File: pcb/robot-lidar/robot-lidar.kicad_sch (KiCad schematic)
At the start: 1 part, among them U1 STM32F429VETx

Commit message: add jack
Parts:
- added J1: Barrel_Jack, symbol Connector:Barrel_Jack
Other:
- moved on the sheet: U1
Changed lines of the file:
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@@
 (kicad_sch (version 20230121) (generator eeschema)
   (paper "A4")
-  (symbol (lib_id "MCU_ST_STM32F4:STM32F429VETx") (at 90.17 99.06 0) (unit 1)
+  (symbol (lib_id "MCU_ST_STM32F4:STM32F429VETx") (at 77.47 113.03 0) (unit 1)
     (in_bom yes) (on_board yes) (dnp no) (fields_autoplaced)
-    (property "Reference" "U1" (at 94.9041 167.64 0)
+    (property "Reference" "U1" (at 82.2041 181.61 0)
       (effects (font (size 1.27 1.27)) (justify left))
     )
-    (property "Value" "STM32F429VETx" (at 94.9041 170.18 0)
+    (property "Value" "STM32F429VETx" (at 82.2041 184.15 0)
       (effects (font (size 1.27 1.27)) (justify left))
     )
-    (property "Footprint" "Package_QFP:LQFP-100_14x14mm_P0.5mm" (at 72.39 165.1 0)
+    (property "Footprint" "Package_QFP:LQFP-100_14x14mm_P0.5mm" (at 59.69 179.07 0)
       (effects (font (size 1.27 1.27)) (justify right) hide)
     )
-    (property "Datasheet" "https://www.st.com/resource/en/datasheet/stm32f429ve.pdf" (at 90.17 99.06 0)
+    (property "Datasheet" "https://www.st.com/resource/en/datasheet/stm32f429ve.pdf" (at 77.47 113.03 0)
       (effects (font (size 1.27 1.27)) hide)
     )
@@
         )
       )
+    )
+  )
+  (symbol (lib_id "Connector:Barrel_Jack") (at 22.86 24.13 0) (unit 1)
+    (in_bom yes) (on_board yes) (dnp no) (fields_autoplaced)
+    (property "Reference" "J1" (at 22.86 15.24 0)
+      (effects (font (size 1.27 1.27)))
+    )
+    (property "Value" "Barrel_Jack" (at 22.86 17.78 0)
+      (effects (font (size 1.27 1.27)))
+    )
+    (property "Footprint" "" (at 24.13 25.146 0)
+      (effects (font (size 1.27 1.27)) hide)
+    )
+    (property "Datasheet" "~" (at 24.13 25.146 0)
+      (effects (font (size 1.27 1.27)) hide)
+    )
+    (pin "1")
+    (pin "2")
+    (instances
+      (project "robot-lidar"
+        (path "/cb10bbf7-c2c1-4a0d-8947-ad707931d83b"
+          (reference "J1") (unit 1)
+        )
+      )

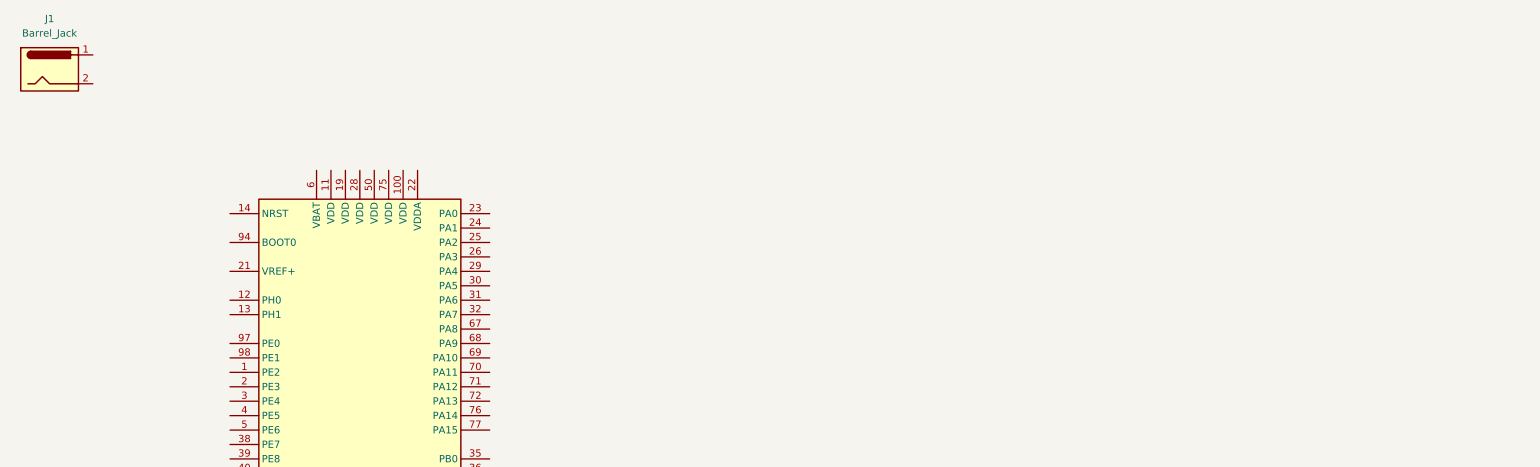
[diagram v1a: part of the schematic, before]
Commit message: add libar + regulator
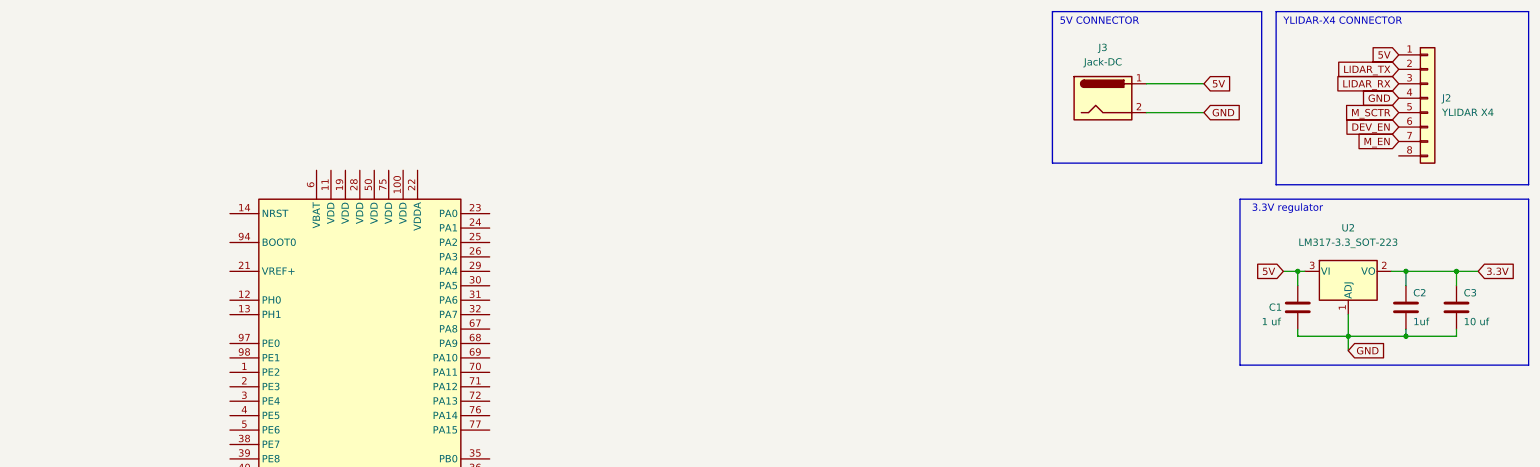
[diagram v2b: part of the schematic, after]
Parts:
- removed J1: Barrel_Jack, symbol Connector:Barrel_Jack
- added C1: 1 uf, Capacitor_SMD:C_0603_1608Metric, symbol Device:C
- added C2: 1uf, Capacitor_SMD:C_0603_1608Metric, symbol Device:C
- added C3: 10 uf, Capacitor_SMD:C_0603_1608Metric, symbol Device:C
- added J2: YLIDAR X4, Connector_Hirose:Hirose_DF13-08P-1.25DSA_1x08_P1.25mm_Vertical, symbol Connector_Generic:Conn_01x08
- added J3: Jack-DC, Connector_BarrelJack:BarrelJack_Horizontal, symbol Connector:Jack-DC
- added U2: LM317-3.3_SOT-223, Package_TO_SOT_SMD:SOT-223-3_TabPin2, symbol Regulator_Linear:LM317_SOT-223
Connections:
- new net 3.3V: C2.1, C3.1, U2.2 (VO)
- new net 5V: C1.1, J2.1 (Pin_1), J3.1, U2.3 (VI)
- new net DEV_EN: J2.6 (Pin_6)
- new net GND: C1.2, C2.2, C3.2, J2.4 (Pin_4), J3.2, U2.1 (ADJ)
- new net LIDAR_RX: J2.3 (Pin_3)
- new net LIDAR_TX: J2.2 (Pin_2)
- new net M_EN: J2.7 (Pin_7)
- new net M_SCTR: J2.5 (Pin_5)
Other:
- note added: "3.3V regulator"
- note added: "5V CONNECTOR"
- note added: "YLIDAR-X4 CONNECTOR"

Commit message: add gyro
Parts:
- added C1, C2, C3: C, Capacitor_SMD:C_0603_1608Metric, symbol Device:C
- added C4, C5, C6, C7, C8: 1 uf, Capacitor_SMD:C_0603_1608Metric, symbol Device:C
- added R1, R2: R_Small, Resistor_SMD:R_0603_1608Metric, symbol Device:R_Small
- added U2: MPU-6050, Sensor_Motion:InvenSense_QFN-24_4x4mm_P0.5mm, symbol Sensor_Motion:MPU-6050
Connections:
- net GND: now also C1.1, C2.2, C3.2, C4.2, C5.2, C6.2, C7.2, C8.2, U2.1 (CLKIN), U2.11 (FSYNC), U2.18 (GND), U2.9 (AD0)
- net at U1.100 (VDD): now also U1.11 (VDD), U1.19 (VDD), U1.22 (VDDA), U1.28 (VDD), U1.50 (VDD), U1.75 (VDD), C4.1, C5.1, C6.1, C7.1, C8.1
- new net: C3.1, U2.20 (CPOUT)
- new net: C2.1, U2.10 (REGOUT)
- new net +3V3: C1.2, R1.1, R2.1, U2.13 (VDD), U2.8 (VDDIO)
- new net MPU_IRQ: U2.12 (INT)
- new net SCL: R1.2, U2.23 (SCL)
- new net SDA: R2.2, U2.24 (SDA)
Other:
- note added: "MPU6050"

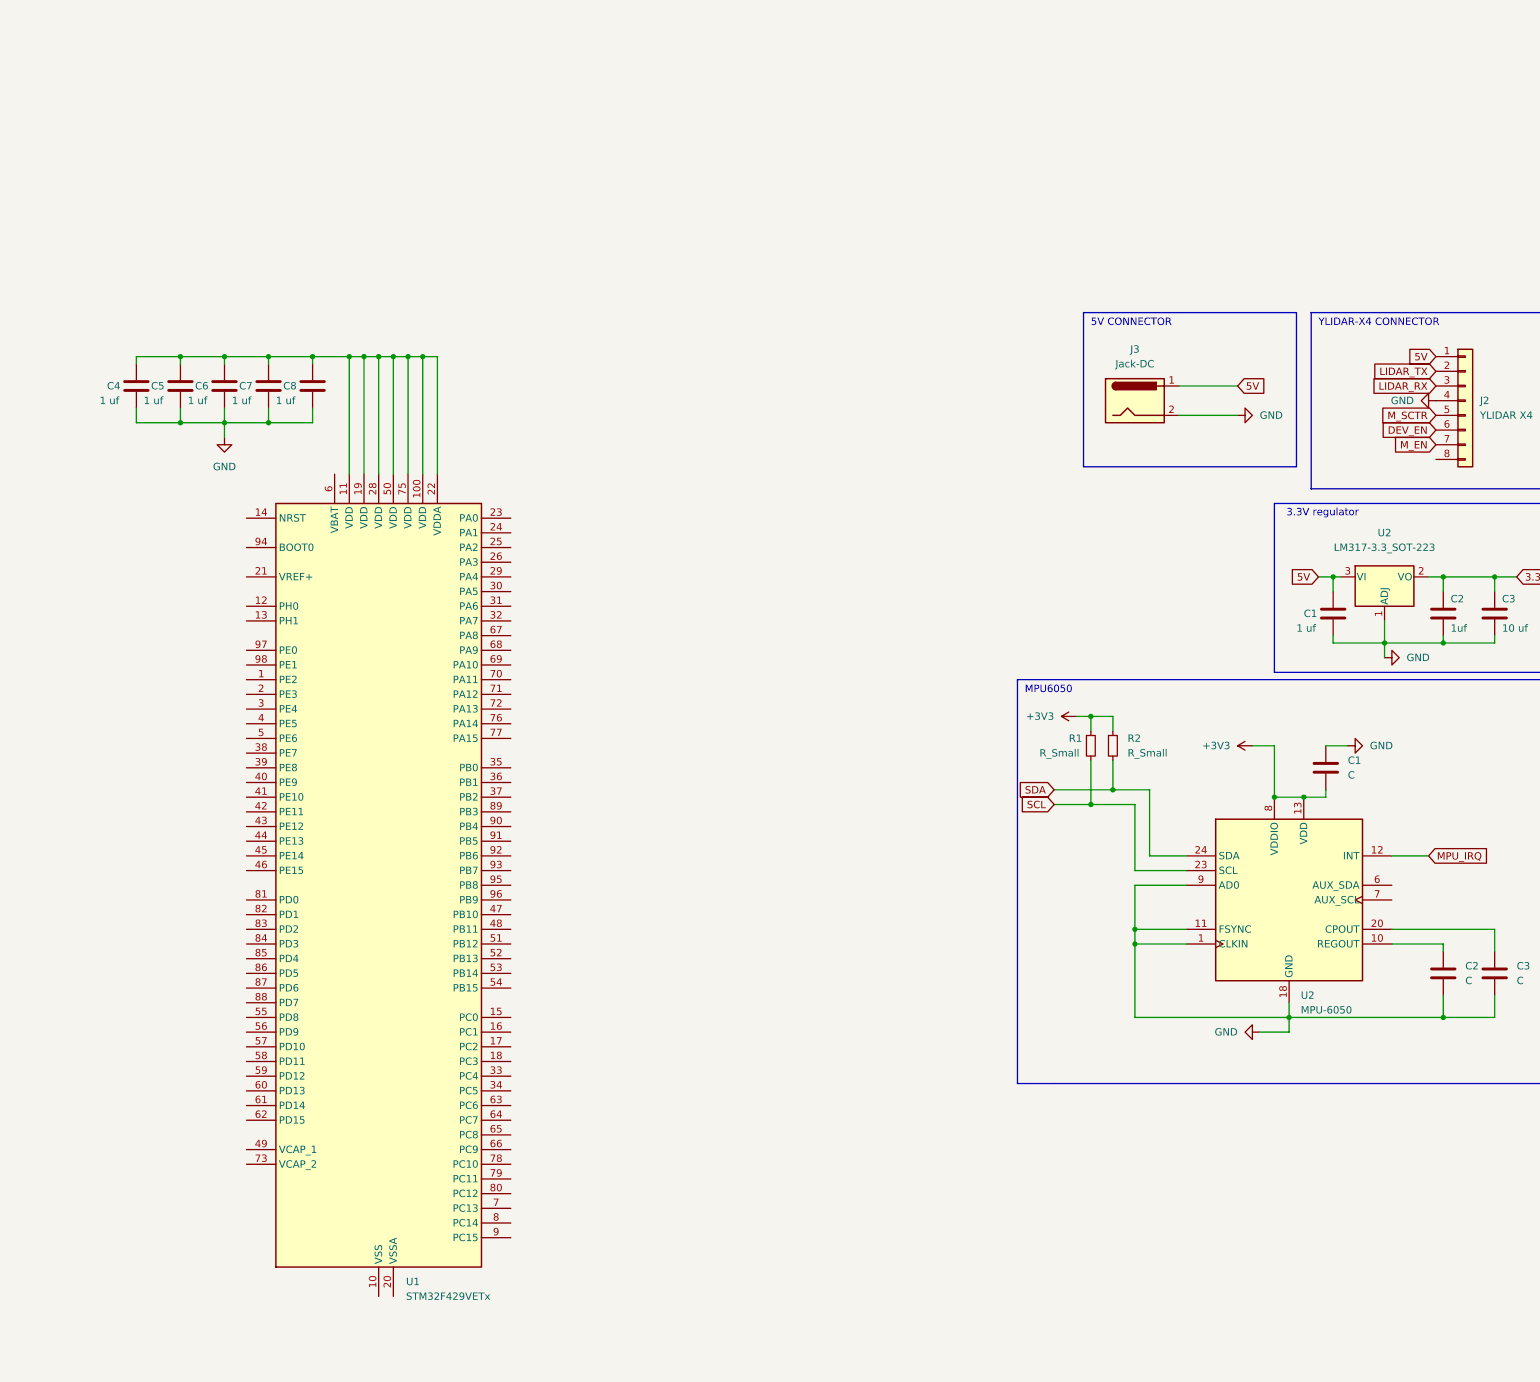
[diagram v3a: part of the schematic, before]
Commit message: add i2c pin + crystal + SWD
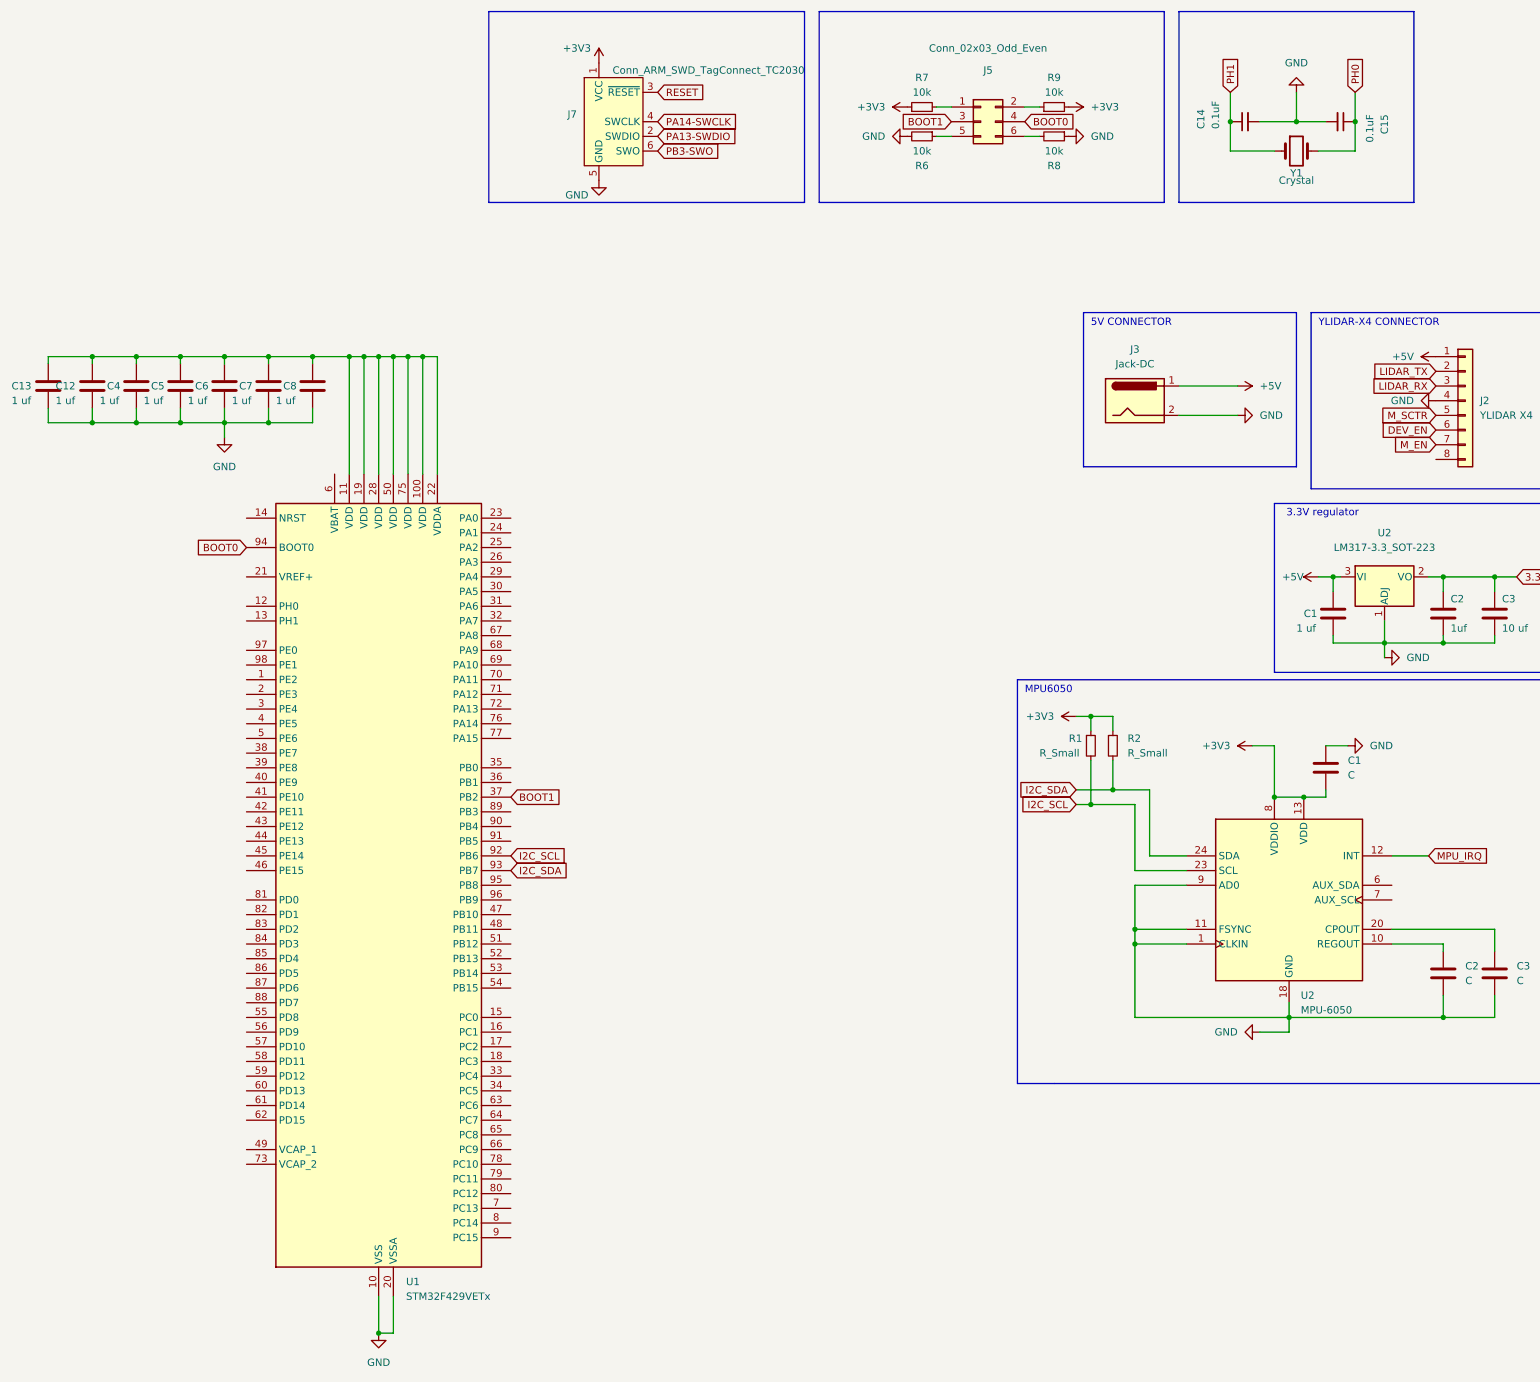
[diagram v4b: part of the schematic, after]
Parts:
- added C12, C13: 1 uf, Capacitor_SMD:C_0603_1608Metric, symbol Device:C
- added C14, C15: 0.1uF, Capacitor_SMD:C_0603_1608Metric, symbol Device:C_Small
- added J5: Conn_02x03_Odd_Even, Connector_PinHeader_2.54mm:PinHeader_2x03_P2.54mm_Vertical_SMD, symbol Connector_Generic:Conn_02x03_Odd_Even
- added J7: Conn_ARM_SWD_TagConnect_TC2030, Connector_PinHeader_2.54mm:PinHeader_1x06_P2.54mm_Vertical, symbol Connector:Conn_ARM_SWD_TagConnect_TC2030
- added R6, R7, R8, R9: 10k, Resistor_SMD:R_0603_1608Metric, symbol Device:R_Small
- added Y1: Crystal, Crystal:Crystal_SMD_HC49-SD, symbol Device:Crystal
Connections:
- net SCL is gone; now on net I2C_SCL: R1.2, U2.23 (SCL)
- net SDA is gone; now on net I2C_SDA: R2.2, U2.24 (SDA)
- net +3V3: now also J7.1 (VCC), R7.1, R9.2
- net GND: now also U1.10 (VSS), U1.20 (VSSA), U1.27 (VSS), U1.74 (VSS), U1.99 (VSS), C12.2, C13.2, C14.2, C15.2, J7.5 (GND), R6.2, R8.1
- net at C4.1, C5.1, C6.1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: now also C12.1, C13.1
- net BOOT1: now reaches U1.37 (PB2)
- net BOOT1: now also J5.3 (Pin_3)
- net I2C_SCL: now reaches U1.92 (PB6)
- net I2C_SDA: now reaches U1.93 (PB7)
- net BOOT0: now reaches U1.94 (BOOT0)
- net BOOT0: now also J5.4 (Pin_4)
- net 5V renamed +5V
- new net: J5.5 (Pin_5), R6.1
- new net: J5.1 (Pin_1), R7.2
- new net: J5.2 (Pin_2), R9.1
- new net: J5.6 (Pin_6), R8.2
- new net PA13-SWDIO: J7.2 (SWDIO)
- new net PA14-SWCLK: J7.4 (SWCLK)
- new net PB3-SWO: J7.6 (SWO)
- new net PH0: C15.1, Y1.2
- new net PH1: C14.1, Y1.1
- new net RESET: J7.3 (~{RESET})
